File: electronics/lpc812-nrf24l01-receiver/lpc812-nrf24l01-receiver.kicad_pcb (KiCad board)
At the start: 2 copper layers, 29.2 x 26.7 mm, 16 parts, among them K1 BAT, K2 CH3, K3 TH, K4 ST, P1 NRF24L01+, SW1 ISP/BIND, U1 MCP1703T-3302E/CB, U2 LPC812M101JDH16_TSSOP16, X1 12 MHz

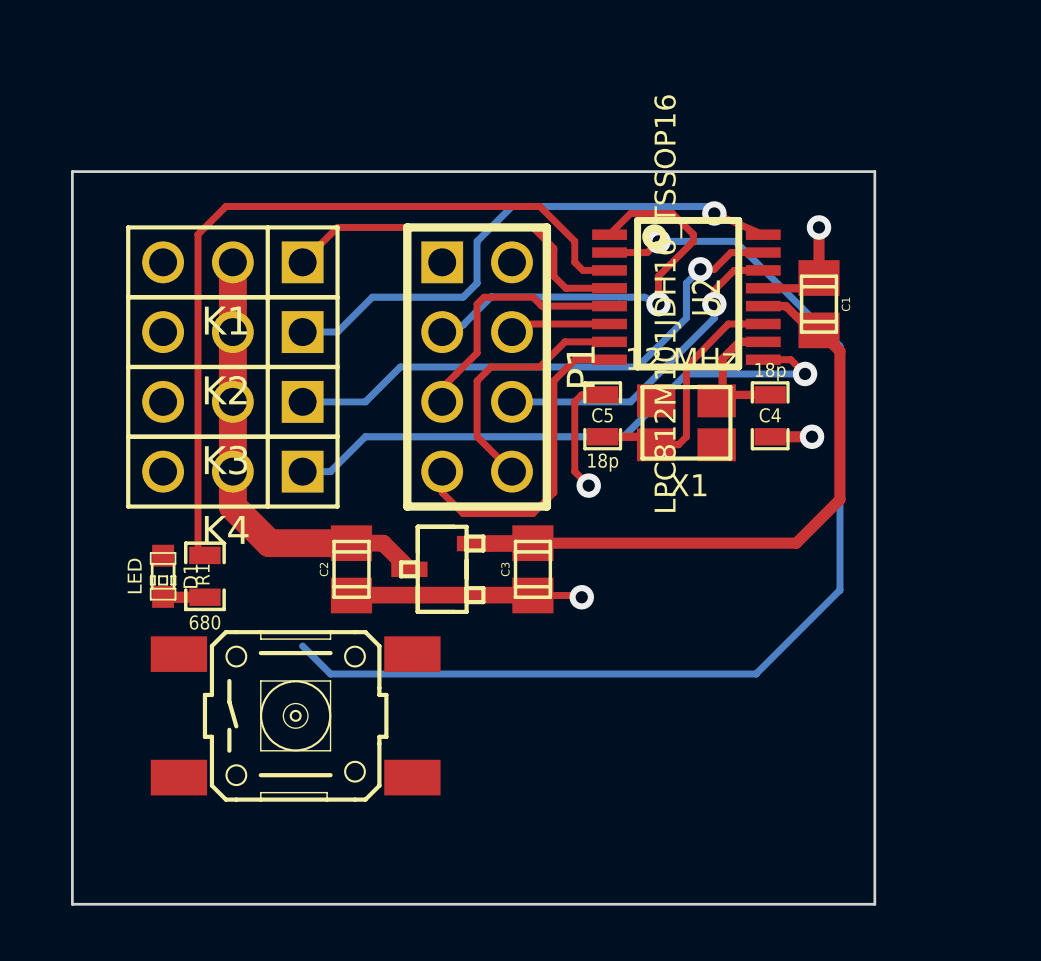
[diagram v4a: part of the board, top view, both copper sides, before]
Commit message: Change pin-out for better layout
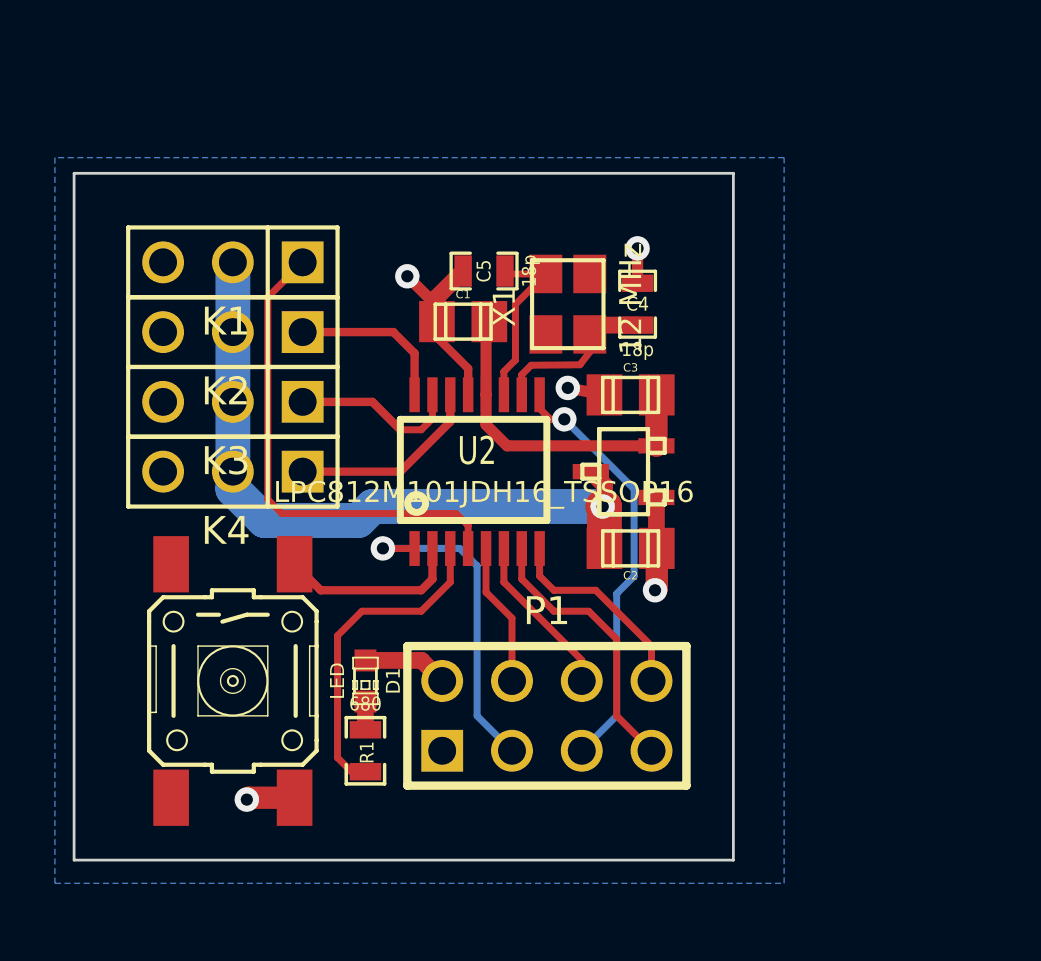
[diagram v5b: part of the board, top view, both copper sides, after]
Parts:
- moved C1 13.0 mm to (26.2, 17.4), turned to 0 degrees
- moved P1 13.0 mm to (29.2, 31.8), turned to 0 degrees
- moved C2 10.2 mm to (32.3, 25.7), turned to 180 degrees
- moved U2 9.92 mm to (26.7, 22.9), turned to 0 degrees
- moved R1 8.63 mm to (22.6, 33.0), turned to 270 degrees
- moved D1 8.29 mm to (22.6, 30.5)
- moved U1 7.50 mm to (32.0, 22.9)
- moved C3 7.28 mm to (32.3, 20.1), turned to 0 degrees
- moved C5 6.81 mm to (26.9, 15.6), turned to 180 degrees
- moved C4 6.31 mm to (32.5, 16.8), turned to 90 degrees
- moved X1 6.11 mm to (30.0, 16.8), turned to 90 degrees
- moved SW1 2.62 mm to (17.8, 30.5), turned to 270 degrees
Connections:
- U2 pad 14: MOSI -> CH1
- U2 pad 5: SCK -> CSN
- U2 pad 6: CSN -> MOSI
- U2 pad 7: IRQ -> MISO
- U2 pad 8: MISO -> IRQ
- U2 pad 9: CH1 -> SCK
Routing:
- net ISP/BIND: track 40.3 -> 6.69 mm, vias 1 -> 0
- net LED: track 28.6 -> 11.8 mm
- net CH1: track 21.5 -> 7.11 mm, vias 1 -> 0
- net CH3/Rx: track 19.8 -> 5.90 mm, vias 1 -> 0
- net CH2: track 19.8 -> 6.18 mm, vias 1 -> 0
- net +BATT: track 16.3 -> 27.0 mm, vias 0 -> 1
- net +3.3V: track 22.8 -> 15.3 mm
- net SCK: track 9.14 -> 15.5 mm, vias 0 -> 1
- net MOSI: track 11.7 -> 6.00 mm, vias 1 -> 0
- net CH4/CPPM/Tx: track 13.2 -> 17.7 mm
- net VSS: track 18.3 -> 15.3 mm, vias 4 -> 5
- net CE: track 15.2 -> 12.1 mm
- net N-0000018: track 9.29 -> 6.56 mm
- net IRQ: track 9.24 -> 7.40 mm
- net MISO: track 11.9 -> 10.1 mm
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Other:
- board size 29.2 x 26.7 mm -> 24 x 25 mm

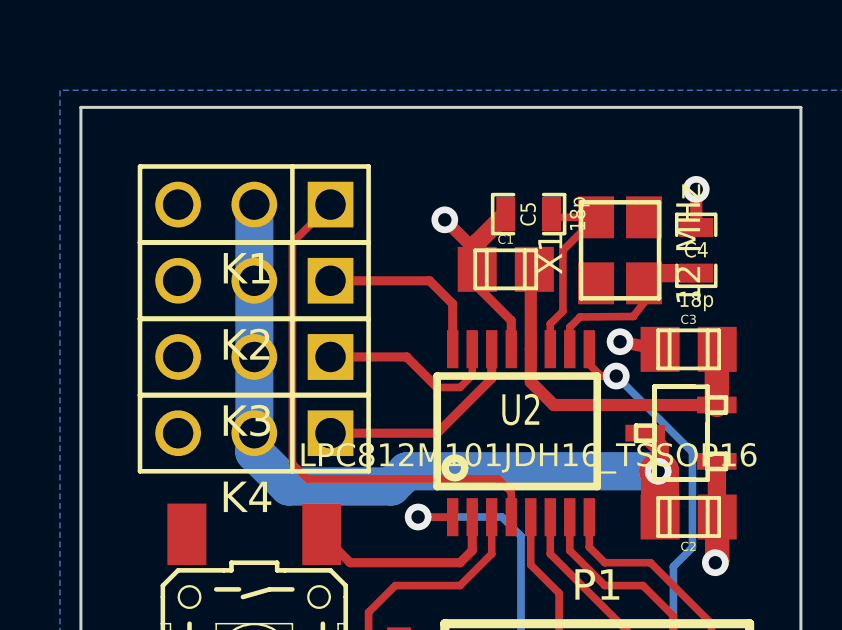
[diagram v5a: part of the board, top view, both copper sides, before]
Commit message: Make page smaller
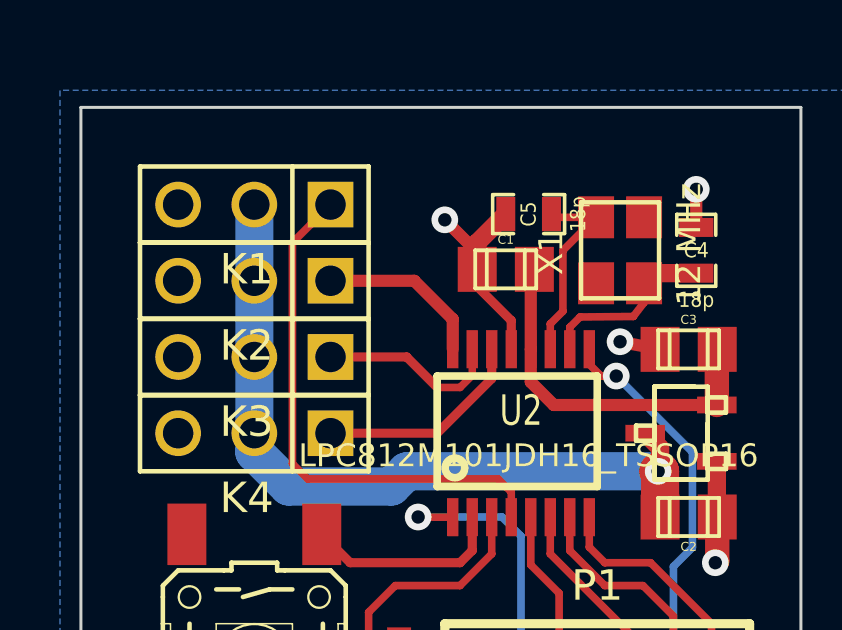
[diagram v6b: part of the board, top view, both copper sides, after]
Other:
- rule via_min_size: 0.889 -> 0.508

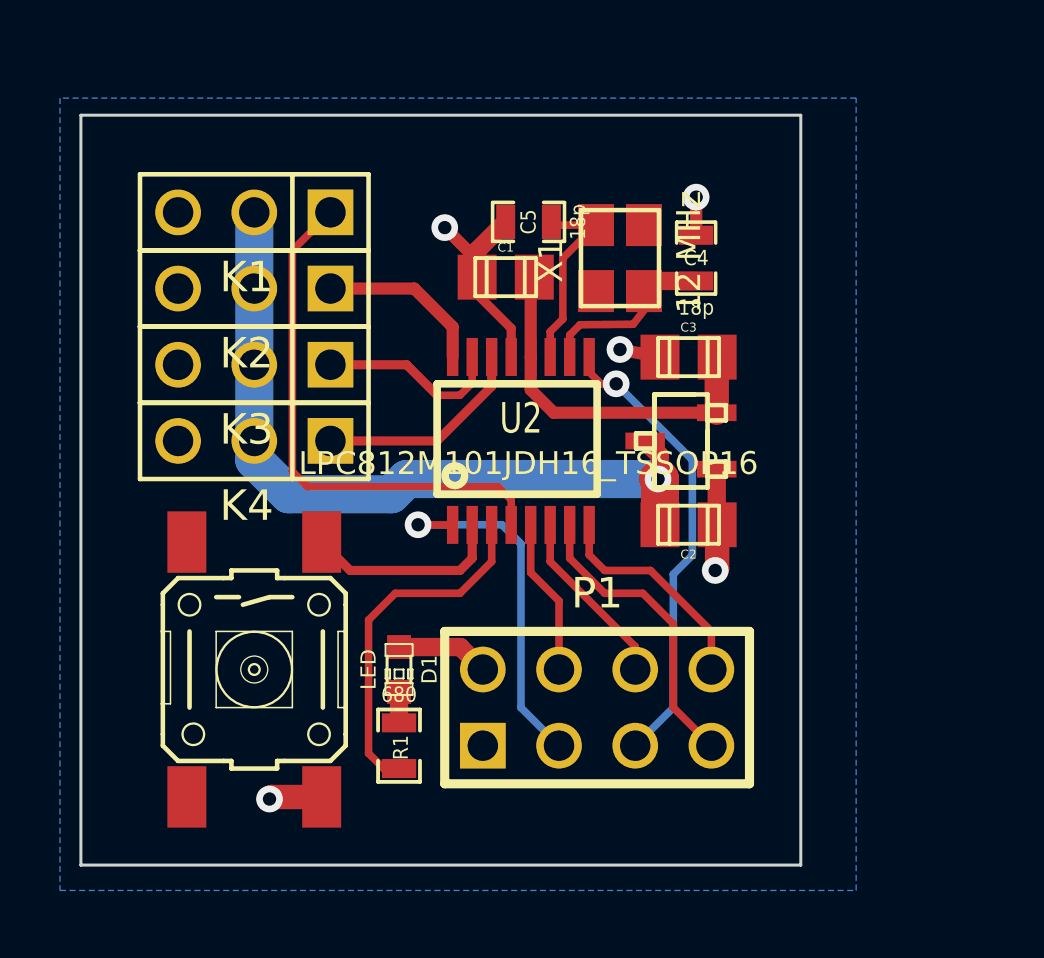
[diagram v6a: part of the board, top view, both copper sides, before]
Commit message: Re-layout the board, add protection resistors
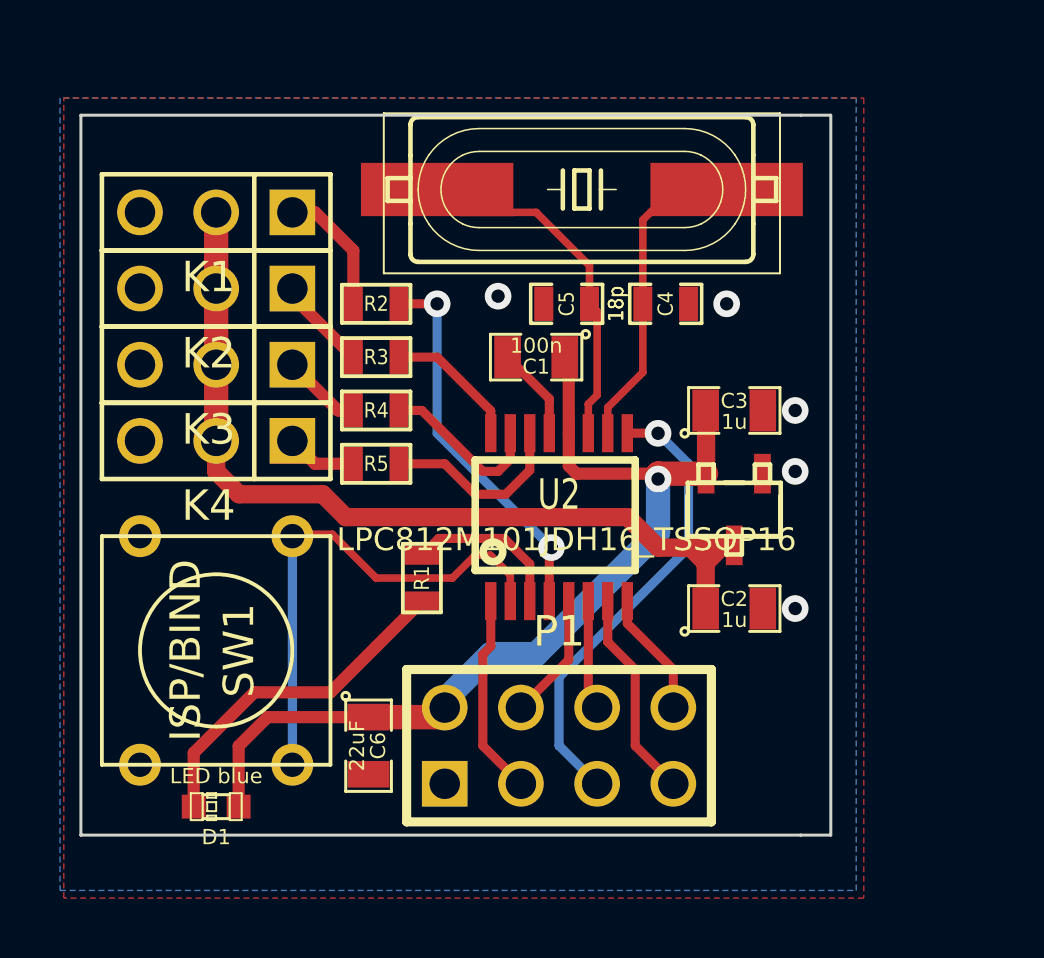
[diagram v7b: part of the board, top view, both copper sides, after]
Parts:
- added C6: 22uF, SM0805, F.Cu at (21.6, 33.0)
- added R2: 680, SM0603, F.Cu at (21.8, 18.3)
- added R3: 680, SM0603, F.Cu at (21.8, 20.1)
- added R4: 680, SM0603, F.Cu at (21.8, 21.8)
- added R5: 680, SM0603, F.Cu at (21.8, 23.6)
- C1, C2, C3: footprint c_0805 -> SM0805
- D1: value LED -> LED blue
- R1: value 680 -> 270; footprint SM0603_Resistor -> SM0603
- SW1: footprint switches-B3S-10XX -> SW_PUSH_SMALL
- X1: footprint crystal_FA238-TSX3225 -> crystal-SM49
- moved D1 7.62 mm to (16.5, 35.1), turned to 180 degrees
- moved R1 5.64 mm to (23.4, 27.4), turned to 90 degrees
- moved C2 3.18 mm to (33.8, 28.4), turned to 0 degrees
- moved C5 3.01 mm to (28.2, 18.3)
- moved U1 2.90 mm to (33.8, 25.1), turned to 180 degrees
- moved C1 2.85 mm to (27.2, 20.1), turned to 180 degrees
- moved U2 2.84 mm to (27.9, 25.4)
- moved X1 2.62 mm to (28.7, 14.5), turned to 180 degrees
- moved C3 2.34 mm to (33.8, 21.8)
- moved C4 1.83 mm to (31.5, 18.3), turned to 0 degrees
- moved P1 1.80 mm to (27.9, 33.0)
- moved SW1 1.42 mm to (16.5, 29.8)
- moved K1 1.27 mm to (16.5, 15.2)
- moved K2 1.27 mm to (16.5, 17.8)
- moved K3 1.27 mm to (16.5, 20.3)
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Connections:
- K1 pad 1: CH4/CPPM/Tx -> N-000004
- K2 pad 1: CH3/Rx -> N-000001
- K3 pad 1: CH2 -> N-000003
- K4 pad 1: CH1 -> N-000002
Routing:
- net +3.3V: track 15.3 -> 31.9 mm, vias 0 -> 1
- net VSS: track 15.3 -> 3.13 mm, vias 5 -> 0
- net N-0000019: track 1.03 -> 11.5 mm
- net ISP/BIND: track 6.69 -> 17.0 mm
- net LED: track 11.8 -> 5.47 mm
- net N-0000022: track 6.56 -> 11.9 mm
- net CE: track 12.1 -> 6.73 mm, vias 1 -> 0
- net N-0000021: track 6.10 -> 10.8 mm
- net CH4/CPPM/Tx: track 17.7 -> 13.1 mm, vias 0 -> 2
- net +BATT: track 27.0 -> 31.3 mm, vias 1 -> 0
- net N-000004: track 0.00 -> 4.34 mm
- net IRQ: track 7.40 -> 4.19 mm
- net N-000001: track 0.00 -> 3.13 mm
- net MISO: track 10.1 -> 7.00 mm
- net N-000003: track 0.00 -> 2.66 mm
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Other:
- board size 24 x 25 mm -> 25 x 24 mm

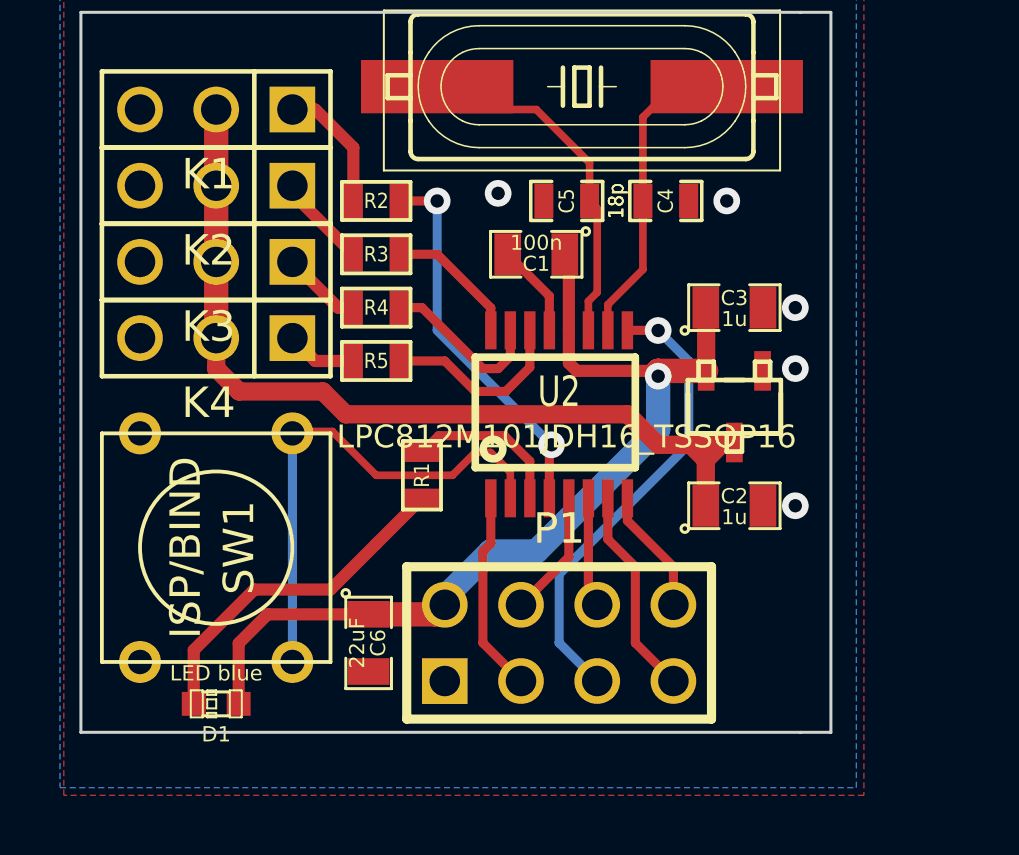
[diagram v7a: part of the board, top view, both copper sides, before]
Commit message: Tweak the board and use NXP footprints
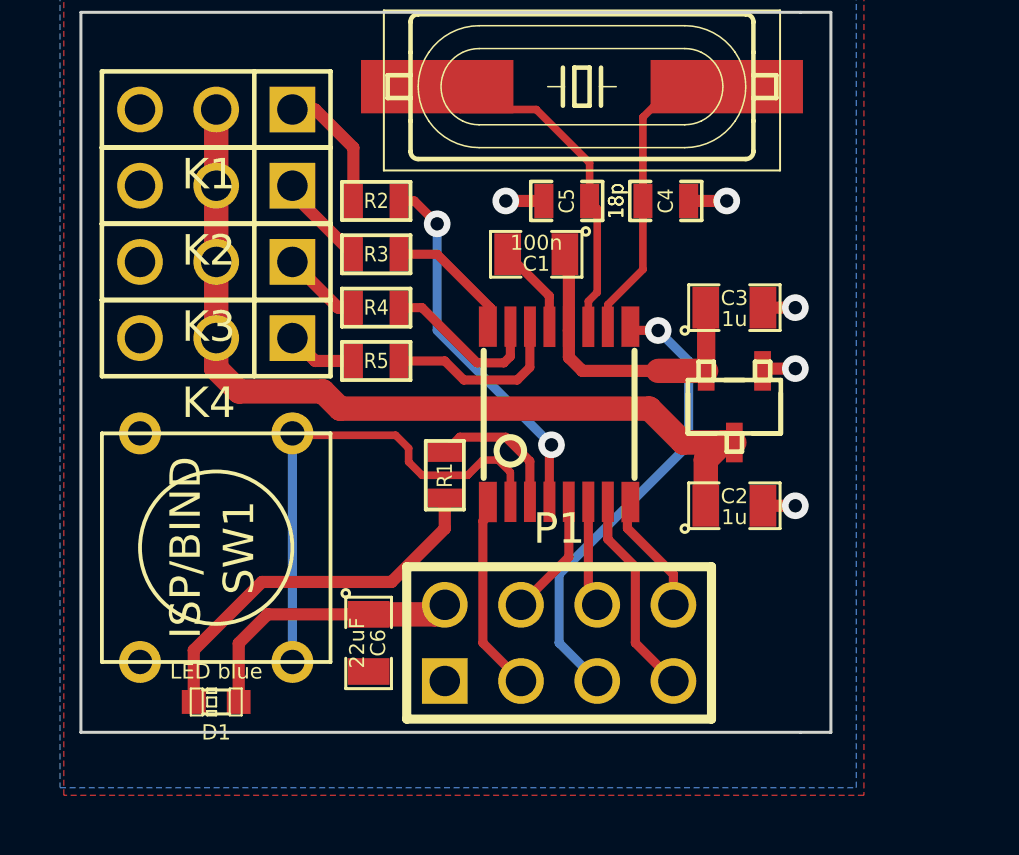
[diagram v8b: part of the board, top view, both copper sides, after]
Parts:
- U2: footprint TSSOP16 -> NXP-TSSOP16
- moved R1 0.76 mm to (24.1, 27.4)
- moved D1 0.06 mm to (16.5, 35.0)
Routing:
- net +3.3V: track 31.9 -> 20.0 mm, vias 1 -> 0
- net VSS: track 3.13 -> 8.95 mm, vias 0 -> 5
- net +BATT: track 31.3 -> 29.3 mm
- net N-0000019: track 11.5 -> 12.8 mm
- net LED: track 5.47 -> 4.66 mm
- net (no net): vias 5 -> 0
